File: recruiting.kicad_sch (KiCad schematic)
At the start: 1 part

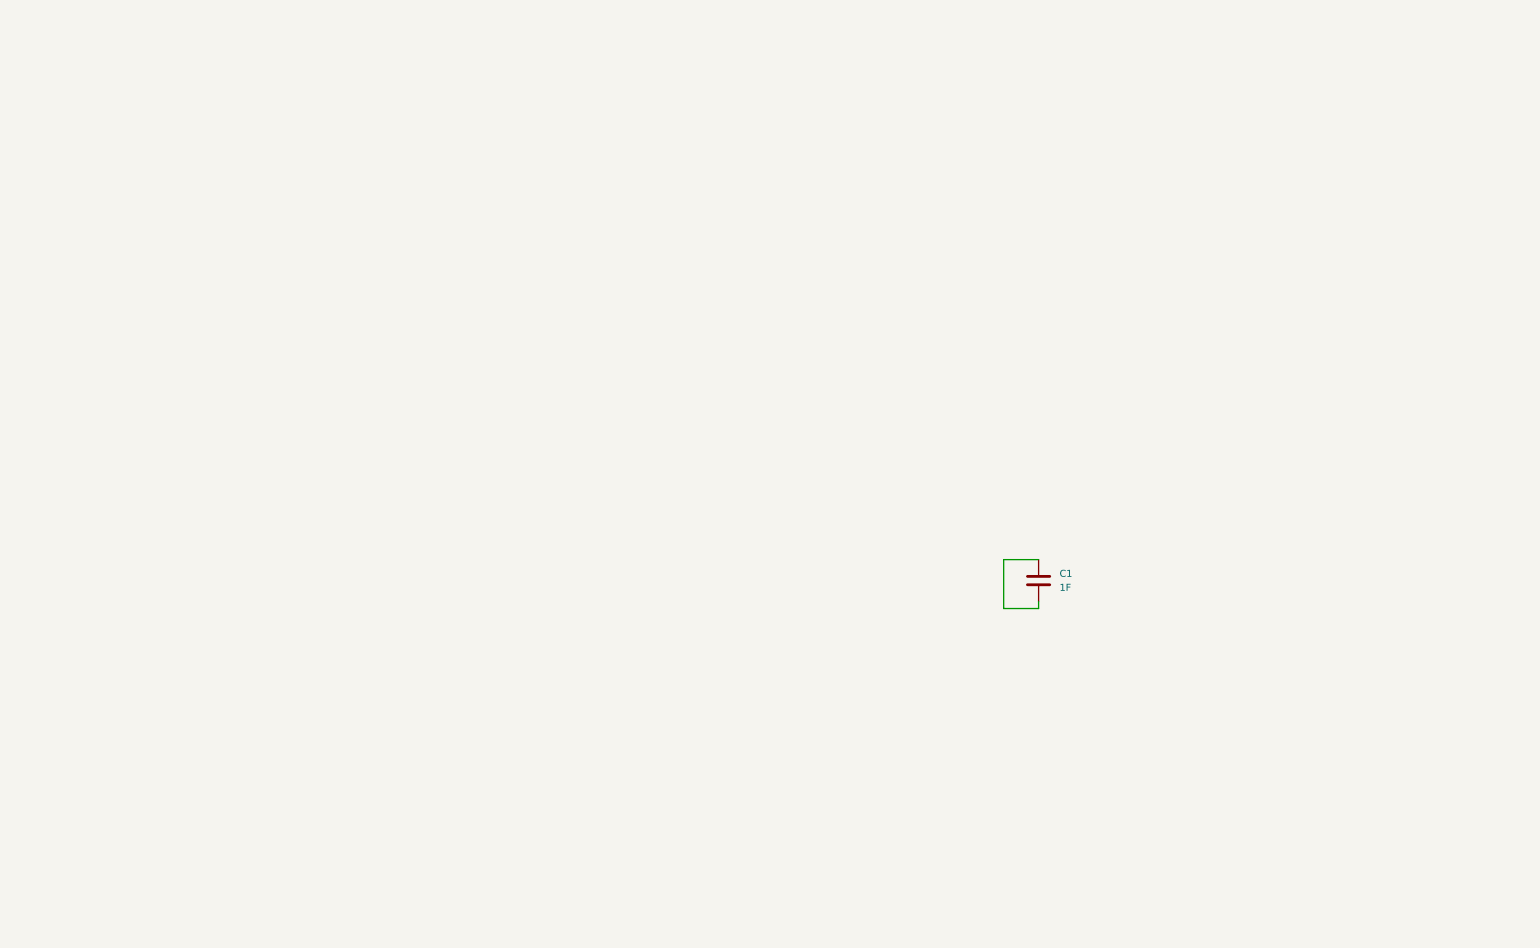
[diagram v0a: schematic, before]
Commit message: fatti alcuni calcoli secondo datasheet per il dimensionamento delle resistenze Rfb1/2 e dimensionamento del MOSFET a canale P per lo switch
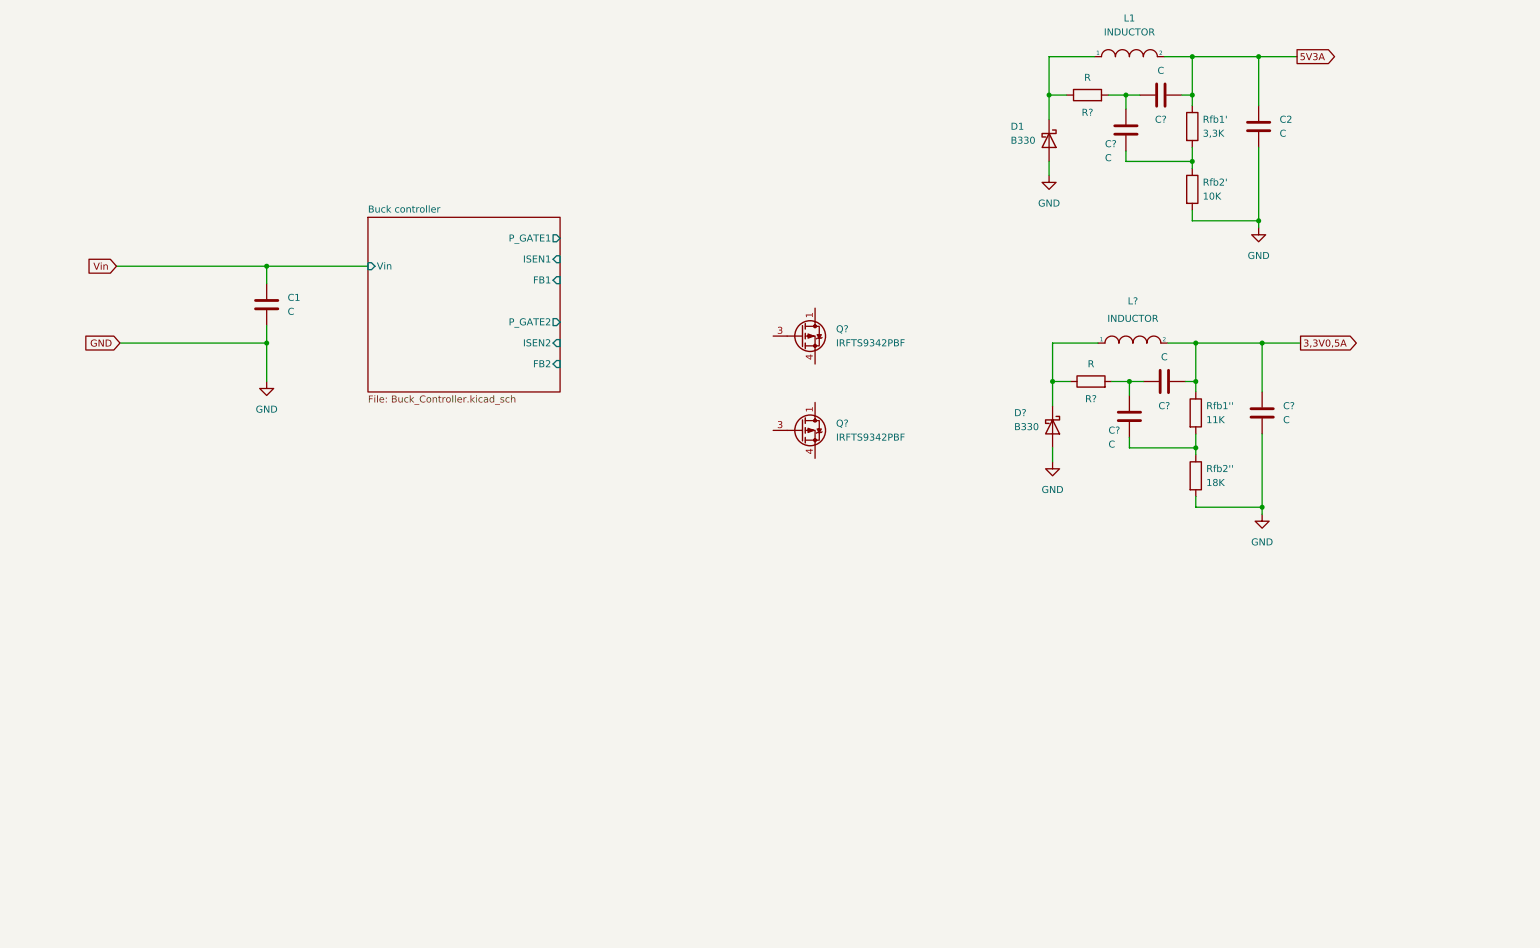
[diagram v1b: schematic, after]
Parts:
- added C2, C? (x5): C, symbol Device:C
- added D1, D?: B330, Diode_SMD:D_SMC, symbol Diode:B330
- added L1, L?: INDUCTOR, symbol pspice:INDUCTOR
- added Q? (x2): IRFTS9342PBF, Package_SO:TSOP-6_1.65x3.05mm_P0.95mm, symbol Transistor_FET:IRFTS9342PBF
- added R? (x2): R, symbol Device:R
- added Rfb1': 3,3K, Resistor_SMD:R_1210_3225Metric, symbol Device:R
- added Rfb1'': 11K, Resistor_SMD:R_1210_3225Metric, symbol Device:R
- added Rfb2': 10K, Resistor_SMD:R_1210_3225Metric, symbol Device:R
- added Rfb2'': 18K, Resistor_SMD:R_1210_3225Metric, symbol Device:R
- C1: value 1F -> C; footprint Capacitor_SMD:C_0805_2012Metric -> (none)
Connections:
- net GND: now reaches C1.2
- net GND: now also C2.2, C?.2, D1.2 (A), D?.2 (A), Rfb2''.2, Rfb2'.2; no longer C1.1
- new net: D?.1 (K), L?.1, R?.1
- new net: D1.1 (K), L1.1, R?.1
- new net: C?.1, C?.1, R?.2 (x2)
- new net: C?.2, Rfb1''.2, Rfb2''.1
- new net: C?.2, Rfb1'.2, Rfb2'.1
- new net: Q?.1 (D), Q?.2 (D), Q?.5 (D), Q?.6 (D) (x2)
- new net 3,3V0,5A: C?.1, C?.2, L?.2, Rfb1''.1
- new net 5V3A: C2.1, C?.2, L1.2, Rfb1'.1
- new net Vin: C1.1
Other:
- added sheet Buck controller (Buck_Controller.kicad_sch)

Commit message: ALCUNE MODIFICHE AL CIRCUITO
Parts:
- added Rsen2 (x2): R, symbol Device:R
- gave numbers to parts that had none: 4
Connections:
- net Vin: now also Rsen2.1, Rsen2.1
- net at D2.1 (K), L2.1, R?.1: now also Q2.1 (D), Q2.2 (D), Q2.5 (D), Q2.6 (D)
- net at D1.1 (K), L1.1, R?.1: now also Q1.1 (D), Q1.2 (D), Q1.5 (D), Q1.6 (D)
- net FB_2: now reaches C?.2, Rfb1''.2, Rfb2''.1
- net FB_1: now reaches C?.2, Rfb1'.2, Rfb2'.1
- net GATE_1: now reaches Q1.3 (G)
- net GATE_1: now also Q2.3 (G)
- net ISEN_1: now reaches Q1.4 (S)
- net ISEN_1: now also Rsen2.2
- net ISEN_2: now reaches Q2.4 (S)
- net ISEN_2: now also Rsen2.2
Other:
- moved on the sheet: C1, C2, C?, D1, D2, L1, L2, Q1, Q2, R?, Rfb1', Rfb1''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

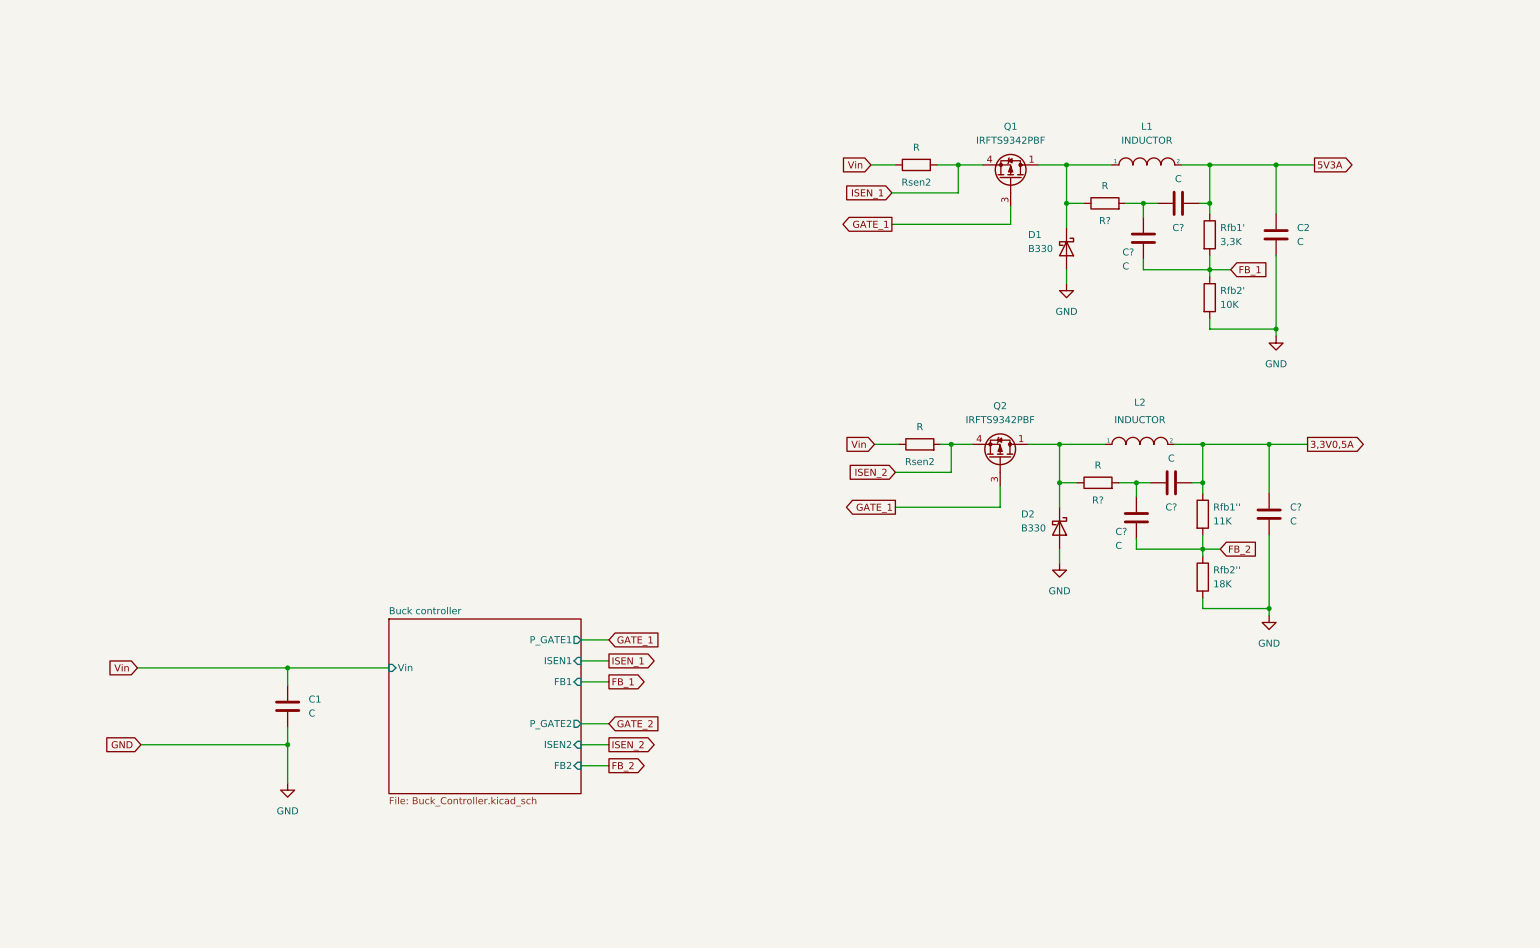
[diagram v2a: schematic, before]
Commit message: aggiunta di un file che esplicita alcuni calcoli
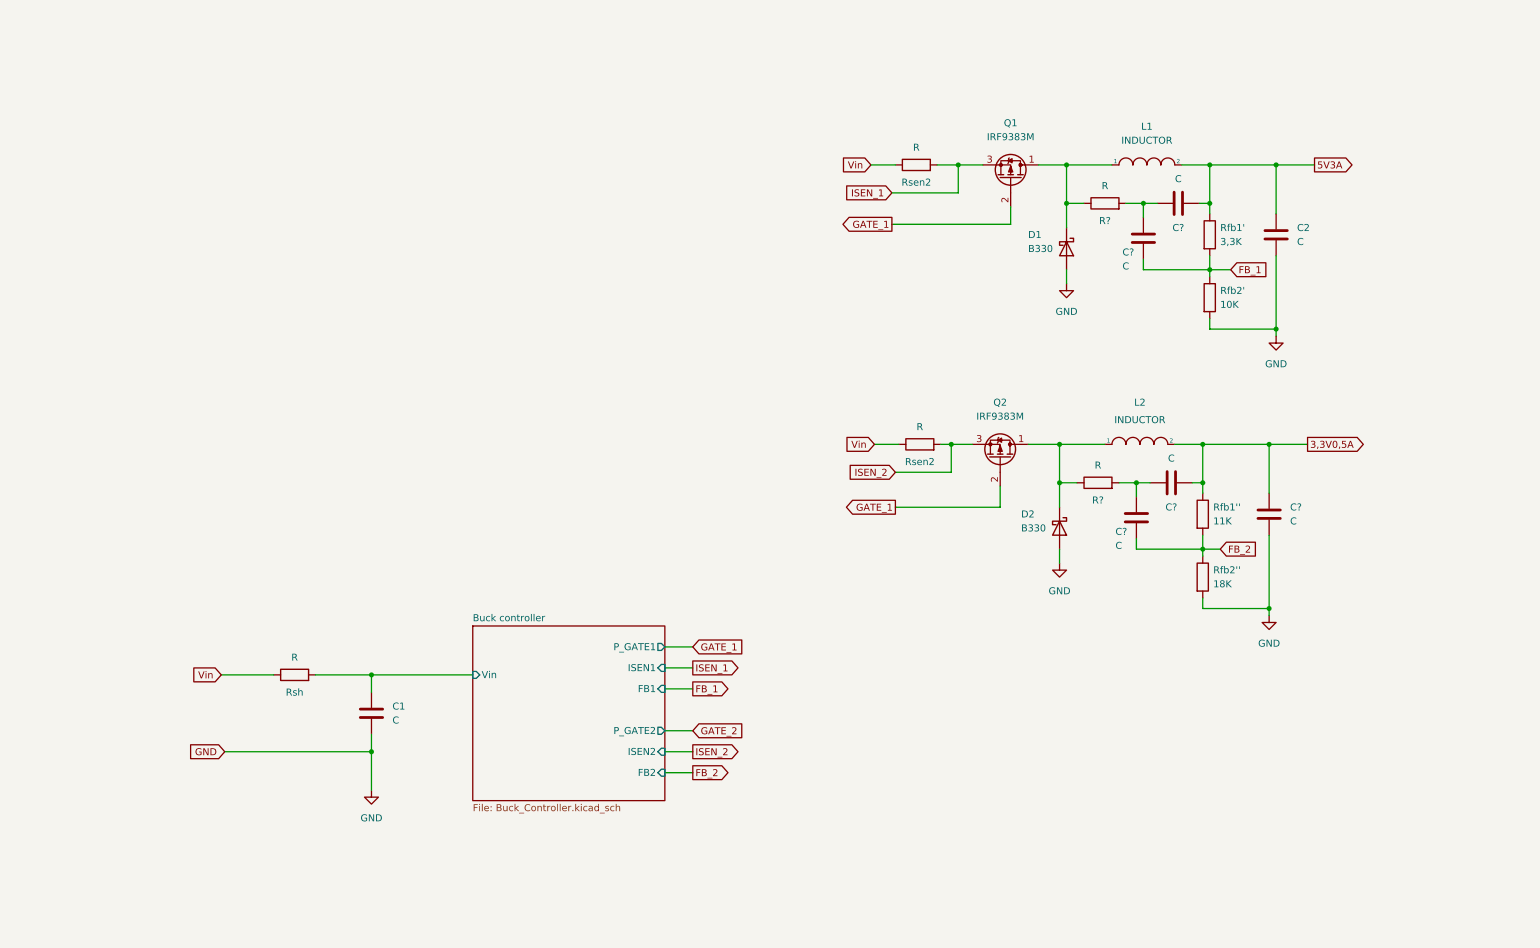
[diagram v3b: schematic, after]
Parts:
- removed Q1, Q2: IRFTS9342PBF, Package_SO:TSOP-6_1.65x3.05mm_P0.95mm, symbol Transistor_FET:IRFTS9342PBF
- added Q1, Q2: IRF9383M, Package_DirectFET:DirectFET_MX, symbol Transistor_FET:IRF9383M
- added Rsh: R, symbol Device:R
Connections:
- net GATE_1: now also Q1.2 (G), Q2.2 (G)
- net ISEN_1: now also Q1.3 (S)
- net ISEN_2: now also Q2.3 (S)
- net Vin: now also Rsh.1; no longer C1.1
- net at D2.1 (K), L2.1, R?.1: now also Q2.1 (D)
- net at D1.1 (K), L1.1, R?.1: now also Q1.1 (D)
- new net Buck controller/Vin: C1.1, Rsh.2
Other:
- moved on the sheet: C1

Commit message: aggiornato il foglio di calcolo per il dimensionamento dell'alimentatore
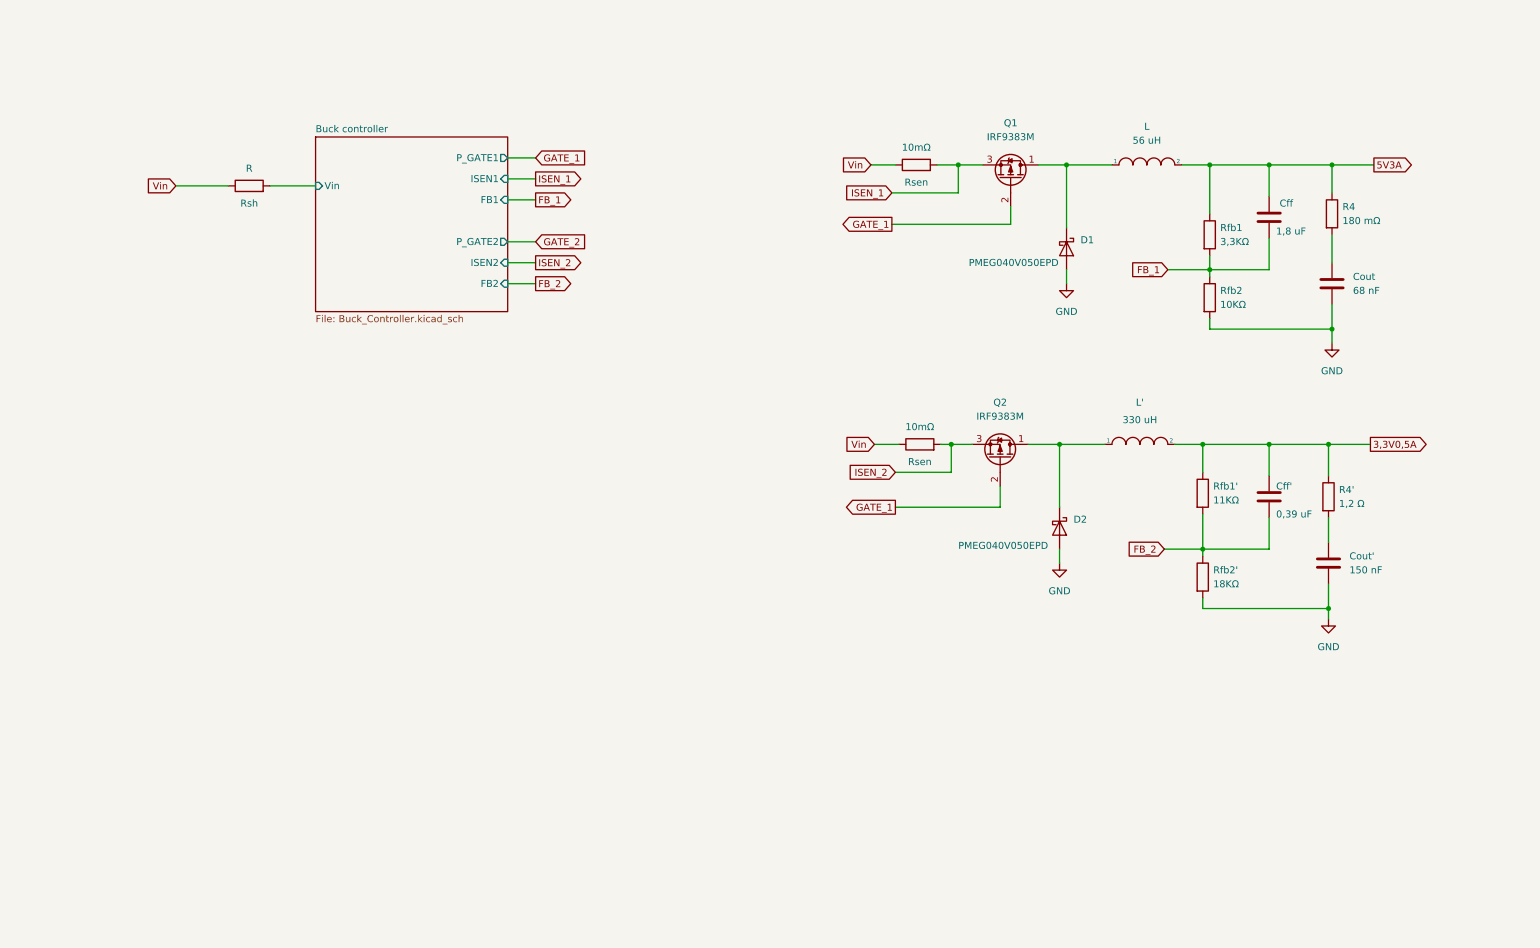
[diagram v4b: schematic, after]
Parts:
- removed C1, C? (x4): C, symbol Device:C
- removed D1, D2: B330, Diode_SMD:D_SMC, symbol Diode:B330
- removed R? (x2): R, symbol Device:R
- added Cff: 1,8 uF, symbol Device:C
- added Cff': 0,39 uF, symbol Device:C
- added D1, D2: PMEG040V050EPD, Package_TO_SOT_SMD:Nexperia_CFP15_SOT-1289, symbol Diode:PMEG040V050EPD
- added R4: 180 mΩ, Resistor_SMD:R_1210_3225Metric, symbol Device:R
- added R4': 1,2 Ω, Resistor_SMD:R_1210_3225Metric, symbol Device:R
- Cout: renamed from C2; value C -> 68 nF
- Cout': renamed from C?; value C -> 150 nF
- L: renamed from L1; value INDUCTOR -> 56 uH
- L': renamed from L2; value INDUCTOR -> 330 uH
- Rfb1: renamed from Rfb1'; value 3,3K -> 3,3KΩ
- Rfb1': renamed from Rfb1''; value 11K -> 11KΩ
- Rfb2: renamed from Rfb2'; value 10K -> 10KΩ
- Rfb2': renamed from Rfb2''; value 18K -> 18KΩ
- Rsen: renamed from Rsen2; value R -> 10mΩ
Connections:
- net 3,3V0,5A: now also Cff'.1, R4'.1; no longer Cout'.1
- net 5V3A: now also Cff.1, R4.1; no longer Cout.1
- net FB_1: now also Cff.2
- net FB_2: now also Cff'.2
- net GND: now also D1.1 (A), D1.2 (A), D2.1 (A), D2.2 (A)
- net at L'.1, Q2.1 (D): now also D2.3 (K)
- net at L.1, Q1.1 (D): now also D1.3 (K)
- new net: Cout.1, R4.2
- new net: Cout'.1, R4'.2
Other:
- moved on the sheet: Cout, Cout', Rfb1', Rsh
